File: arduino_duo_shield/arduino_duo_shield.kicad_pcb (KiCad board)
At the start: 2 copper layers, 102.1 x 119.4 mm, 70 parts, among them J2 EStop, J3 Motor_Control, J4 Limit_Switches, J5 inverter_freq, J6 inverter_cmd, J8 inverter_power, J9 Motor_Control_Mirror, K2 JQC-3F, K3 JQC-3F, P10 Digital, P11 PWM, P12 PWM, P13 Communication, P7 Power, P8 Analog, P9 Analog, Q3 2N7000, Q4 BS250, Q5 2N7000, Q6 2N7000, SW1 SW_Push, U1 4504, U2 4504, U4 74HC14, U6 74HC14, U7 PC817, U8 PC817, U9 PC817

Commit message: Generate gerber files for 1.0-alpha-1
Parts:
- added D1: LED, LED_THT:LED_D3.0mm, F.Cu at (122.9, 42.2)
- R21: value 10K -> 1K5
- moved R21 8.38 mm to (130.0, 47.2), turned to 90 degrees
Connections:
- R21 pad 1: /Spindle_VFD_Control/I_PWRSAFE -> Net-(D1-Pad1)
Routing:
- net /Spindle_VFD_Control/I_PWRSAFE: track 0.00 -> 17.3 mm
- net Net-(D1-Pad1): track 0.00 -> 9.89 mm
- net Net-(Q3-Pad2): track 25.7 -> 29.2 mm
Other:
- board text added: "ACT"
- board text removed: "EN"
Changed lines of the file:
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@@
     (thickness 1.6)
     (drawings 79)
-    (tracks 549)
+    (tracks 563)
     (zones 0)
-    (modules 70)
-    (nets 132)
+    (modules 71)
+    (nets 133)
   )
   (page A4)
@@
       (drillshape 0)
       (scaleselection 1)
-      (outputdirectory "plot/gerber"))
+      (outputdirectory "plot/1.0-alpha-1/"))
   )
   (net 0 "")
@@
   (net 130 "Net-(R24-Pad2)")
   (net 131 /Spindle_VFD_Control/I_PWRSAFE)
+  (net 132 "Net-(D1-Pad1)")
   (net_class Default "This is the default net class."
     (clearance 0.2)
@@
     (add_net "Net-(C8-Pad1)")
     (add_net "Net-(C9-Pad2)")
+    (add_net "Net-(D1-Pad1)")
     (add_net "Net-(D3-Pad2)")
     (add_net "Net-(D4-Pad2)")
@@
     (add_net /Debounce_x6/SWZmin+)
   )
+  (module LED_THT:LED_D3.0mm (layer F.Cu)
+    (at 122.936 42.164 90)
+    (descr "LED, diameter 3.0mm, 2 pins")
+    (tags "LED diameter 3.0mm 2 pins")
+    (fp_text reference D1 (at 1.27 -2.96 90) (layer F.SilkS) hide
+      (effects (font (size 1 1) (thickness 0.15)))
+    )
+    (fp_text value LED (at 1.27 2.96 90) (layer F.Fab)
+      (effects (font (size 1 1) (thickness 0.15)))
+    )
+    (fp_line (start 3.7 -2.25) (end -1.15 -2.25) (layer F.CrtYd) (width 0.05))
+    (fp_line (start 3.7 2.25) (end 3.7 -2.25) (layer F.CrtYd) (width 0.05))
+    (fp_line (start -1.15 2.25) (end 3.7 2.25) (layer F.CrtYd) (width 0.05))
+    (fp_line (start -1.15 -2.25) (end -1.15 2.25) (layer F.CrtYd) (width 0.05))
+    (fp_line (start -0.29 1.08) (end -0.29 1.236) (layer F.SilkS) (width 0.12))
+    (fp_line (start -0.29 -1.236) (end -0.29 -1.08) (layer F.SilkS) (width 0.12))
+    (fp_line (start -0.23 -1.16619) (end -0.23 1.16619) (layer F.Fab) (width 0.1))
+    (fp_circle (center 1.27 0) (end 2.77 0) (layer F.Fab) (width 0.1))
+    (fp_arc (start 1.27 0) (end 0.229039 1.08) (angle -87.9) (layer F.SilkS) (width 0.12))
+    (fp_arc (start 1.27 0) (end 0.229039 -1.08) (angle 87.9) (layer F.SilkS) (width 0.12))
+    (fp_arc (start 1.27 0) (end -0.29 1.235516) (angle -108.8) (layer F.SilkS) (width 0.12))
+    (fp_arc (start 1.27 0) (end -0.29 -1.235516) (angle 108.8) (layer F.SilkS) (width 0.12))
+    (fp_arc (start 1.27 0) (end -0.23 -1.16619) (angle 284.3) (layer F.Fab) (width 0.1))
+    (pad 2 thru_hole circle (at 2.54 0 90) (size 1.8 1.8) (drill 0.9) (layers *.Cu *.Mask)
+      (net 131 /Spindle_VFD_Control/I_PWRSAFE))
+    (pad 1 thru_hole rect (at 0 0 90) (size 1.8 1.8) (drill 0.9) (layers *.Cu *.Mask)
+      (net 132 "Net-(D1-Pad1)"))
+    (model ${KISYS3DMOD}/LED_THT.3dshapes/LED_D3.0mm.wrl
+      (at (xyz 0 0 0))
+      (scale (xyz 1 1 1))
+      (rotate (xyz 0 0 0))
+    )
+  )
   (module Relay_THT:Relay_SPDT_SANYOU_SRD_Series_Form_C (layer F.Cu)
     (at 162.052 58.42)
@@
   )
   (module Resistor_THT:R_Axial_DIN0207_L6.3mm_D2.5mm_P7.62mm_Horizontal (layer F.Cu)
-    (at 128.016 39.116 270)
+    (at 130.048 47.244 90)
     (descr "Resistor, Axial_DIN0207 series, Axial, Horizontal, pin pitch=7.62mm, 0.25W = 1/4W, length*diameter=6.3*2.5mm^2, http://cdn-reichelt.de/documents/datenblatt/B400/1_4W%23YAG.pdf")
     (tags "Resistor Axial_DIN0207 series Axial Horizontal pin pitch 7.62mm 0.25W = 1/4W length 6.3mm diameter 2.5mm")
@@
       (effects (font (size 1 1) (thickness 0.15)))
     )
-    (fp_text value 10K (at 3.81 2.37 90) (layer F.SilkS)
+    (fp_text value 1K5 (at 3.81 2.37 90) (layer F.SilkS)
       (effects (font (size 1 1) (thickness 0.15)))
     )
@@
     (fp_line (start 0.66 1.25) (end 6.96 1.25) (layer F.Fab) (width 0.1))
     (fp_line (start 0.66 -1.25) (end 0.66 1.25) (layer F.Fab) (width 0.1))
-    (pad 2 thru_hole oval (at 7.62 0 270) (size 1.6 1.6) (drill 0.8) (layers *.Cu *.Mask)
+    (pad 2 thru_hole oval (at 7.62 0 90) (size 1.6 1.6) (drill 0.8) (layers *.Cu *.Mask)
       (net 125 "Net-(Q3-Pad2)"))
-    (pad 1 thru_hole circle (at 0 0 270) (size 1.6 1.6) (drill 0.8) (layers *.Cu *.Mask)
-      (net 131 /Spindle_VFD_Control/I_PWRSAFE))
+    (pad 1 thru_hole circle (at 0 0 90) (size 1.6 1.6) (drill 0.8) (layers *.Cu *.Mask)
+      (net 132 "Net-(D1-Pad1)"))
     (model ${KISYS3DMOD}/Resistor_THT.3dshapes/R_Axial_DIN0207_L6.3mm_D2.5mm_P7.62mm_Horizontal.wrl
       (at (xyz 0 0 0))
@@
     )
   )
+  (gr_text ACT (at 119.888 40.64 90) (layer F.SilkS)
+    (effects (font (size 1 1) (thickness 0.15)))
+  )
   (gr_text "Itadinanta CNC Board\nfor Arduino Due\n1.0-alpha-1-2019-12-28" (at 153.416 134.62 90) (layer F.SilkS)
     (effects (font (size 1 1) (thickness 0.15)))
@@
     (effects (font (size 1 1) (thickness 0.15)))
   )
-  (gr_text EN (at 181.864 62.992 90) (layer F.SilkS)
-    (effects (font (size 1 1) (thickness 0.15)))
-  )
   (gr_text NO (at 181.864 49.784 90) (layer F.SilkS)
     (effects (font (size 1 1) (thickness 0.15)))
@@
   (segment (start 146.812 41.656) (end 149.86 38.608) (width 0.25) (layer F.Cu) (net 124))
   (segment (start 138.684 41.656) (end 146.812 41.656) (width 0.25) (layer F.Cu) (net 124))
-  (segment (start 128.016 52.324) (end 128.016 46.736) (width 0.25) (layer F.Cu) (net 125))
   (segment (start 137.684 40.386) (end 136.652 41.418) (width 0.25) (layer F.Cu) (net 125))
   (segment (start 138.684 40.386) (end 137.684 40.386) (width 0.25) (layer F.Cu) (net 125))
   (segment (start 137.684 49.022) (end 138.684 49.022) (width 0.25) (layer F.Cu) (net 125))
-  (segment (start 136.652 47.99) (end 137.684 49.022) (width 0.25) (layer F.Cu) (net 125))
-  (segment (start 128.016 46.736) (end 136.652 46.736) (width 0.25) (layer F.Cu) (net 125))
-  (segment (start 136.652 41.418) (end 136.652 46.736) (width 0.25) (layer F.Cu) (net 125))
   (segment (start 136.652 46.736) (end 136.652 47.99) (width 0.25) (layer F.Cu) (net 125))
+  (segment (start 132.71641 41.656) (end 130.366205 39.305795) (width 0.25) (layer F.Cu) (net 125))
+  (segment (start 136.652 41.656) (end 132.71641 41.656) (width 0.25) (layer F.Cu) (net 125))
+  (segment (start 136.652 41.656) (end 136.652 46.736) (width 0.25) (layer F.Cu) (net 125))
+  (segment (start 136.652 41.418) (end 136.652 41.656) (width 0.25) (layer F.Cu) (net 125))
+  (segment (start 132.08 48.26) (end 136.652 48.26) (width 0.25) (layer F.Cu) (net 125))
+  (segment (start 128.016 52.324) (end 132.08 48.26) (width 0.25) (layer F.Cu) (net 125))
+  (segment (start 136.652 47.99) (end 136.652 48.26) (width 0.25) (layer F.Cu) (net 125))
+  (segment (start 136.652 48.26) (end 137.684 49.022) (width 0.25) (layer F.Cu) (net 125))
   (segment (start 109.22 52.324) (end 113.284 52.324) (width 0.25) (layer F.Cu) (net 126))
   (segment (start 119.997001 45.610999) (end 114.083999 51.524001) (width 0.25) (layer B.Cu) (net 126))
@@
   (segment (start 116.84 60.452) (end 117.348 59.944) (width 0.25) (layer F.Cu) (net 130))
   (segment (start 116.84 63.5) (end 116.84 60.452) (width 0.25) (layer F.Cu) (net 130))
+  (segment (start 138.176 39.116) (end 138.684 39.116) (width 0.25) (layer F.Cu) (net 131))
+  (segment (start 123.835999 38.724001) (end 122.936 39.624) (width 0.25) (layer F.Cu) (net 131))
+  (segment (start 136.668 38.1) (end 124.46 38.1) (width 0.25) (layer F.Cu) (net 131))
+  (segment (start 124.46 38.1) (end 123.835999 38.724001) (width 0.25) (layer F.Cu) (net 131))
+  (segment (start 138.684 39.116) (end 137.684 39.116) (width 0.25) (layer F.Cu) (net 131))
+  (segment (start 137.684 39.116) (end 136.668 38.1) (width 0.25) (layer F.Cu) (net 131))
+  (segment (start 126.866 47.244) (end 128.91663 47.244) (width 0.25) (layer F.Cu) (net 132))
+  (segment (start 122.936 43.314) (end 126.866 47.244) (width 0.25) (layer F.Cu) (net 132))
+  (segment (start 128.91663 47.244) (end 130.048 47.244) (width 0.25) (layer F.Cu) (net 132))
+  (segment (start 122.936 42.164) (end 122.936 43.314) (width 0.25) (layer F.Cu) (net 132))
   (zone (net 1) (net_name GND) (layer B.Cu) (hatch edge 0.508)
     (connect_pads (clearance 0.508))

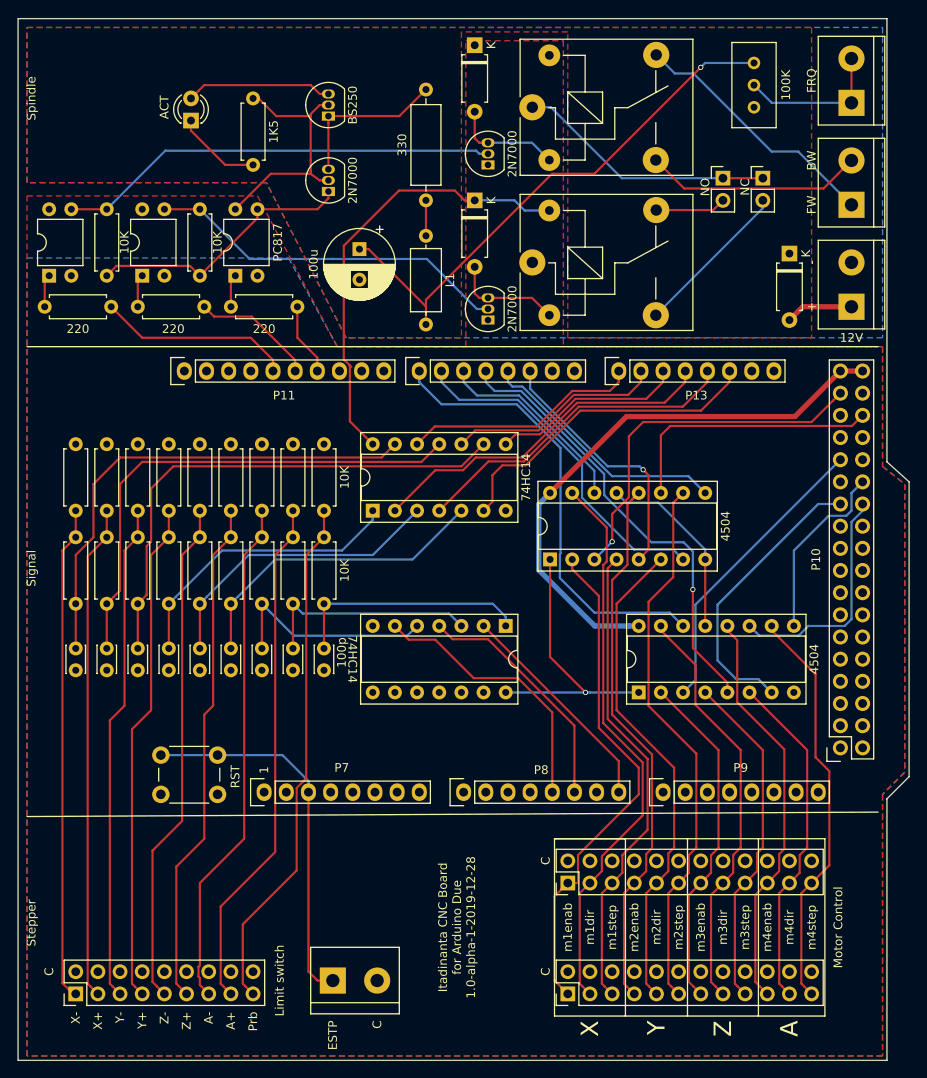
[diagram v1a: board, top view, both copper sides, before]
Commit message: Add voltage follower as end stage of spindle control
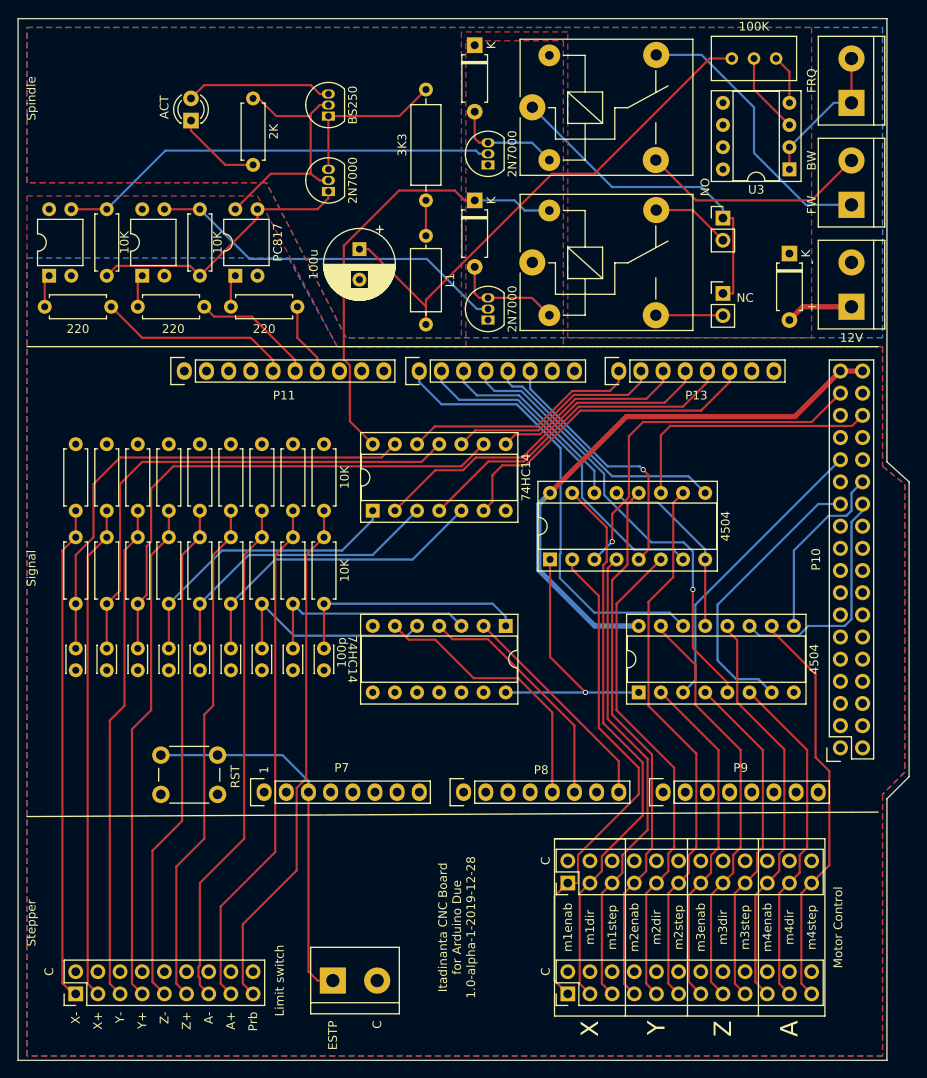
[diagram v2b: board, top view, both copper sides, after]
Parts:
- added U3: LM358, Package_DIP:DIP-8_W7.62mm_Socket, F.Cu at (191.5, 47.8)
- R21: value 1K5 -> 2K
- R23: value 330 -> 3K3
- moved JP2 14.0 mm to (183.9, 62.0)
- moved JP3 4.57 mm to (183.9, 53.3)
- moved RV1 2.59 mm to (184.9, 35.1), turned to 180 degrees
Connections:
- RV1 pad 2: /Spindle_VFD_Control/inverter_frequency_10V -> Net-(RV1-Pad2)
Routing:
- net Net-(JP2-Pad2): track 18.2 -> 7.71 mm
- net Net-(RV1-Pad2): track 0.00 -> 9.30 mm
- net Net-(JP2-Pad1): track 29.8 -> 38.6 mm
- net /Spindle_VFD_Control/inverter_gnd: track 31.4 -> 37.1 mm
- net /Spindle_VFD_Control/inverter_fw_switch: track 29.5 -> 32.6 mm
- net Net-(C8-Pad1): track 62.0 -> 59.7 mm, vias 1 -> 0
- net /Spindle_VFD_Control/inverter_bw_switch: track 25.1 -> 26.2 mm
- net Net-(JP3-Pad2): track 8.10 -> 9.08 mm

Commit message: Expose raw analog frequency control
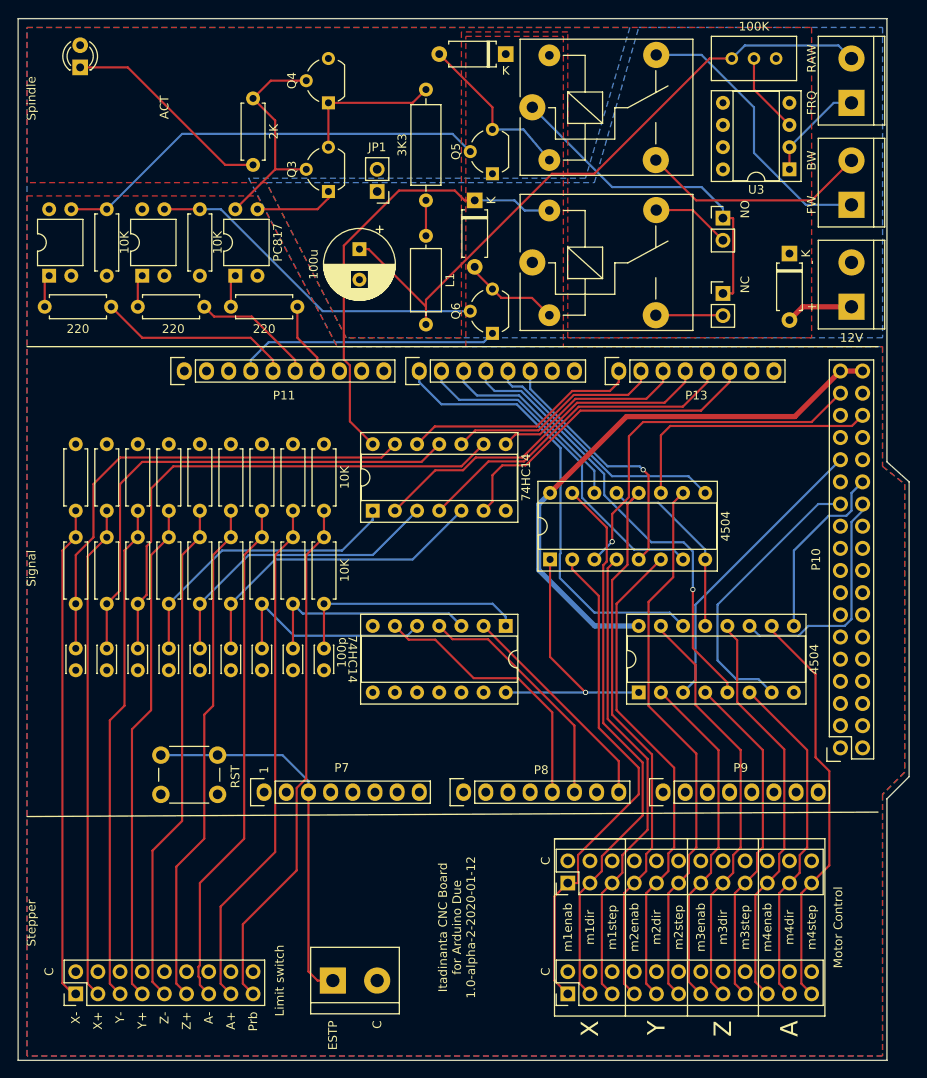
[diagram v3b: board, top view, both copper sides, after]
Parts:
- added JP1: Jumper_NC_Small, Connector_PinHeader_2.54mm:PinHeader_1x02_P2.54mm_Vertical, F.Cu at (144.3, 50.3)
- Q3, Q4, Q5, Q6: footprint Package_TO_SOT_THT:TO-92_Inline -> Package_TO_SOT_THT:TO-92_Wide
- moved D1 14.1 mm to (110.2, 36.1)
- moved D3 3.70 mm to (159.0, 34.5), turned to 180 degrees
- moved Q6 1.61 mm to (157.5, 66.5)
- moved Q4 1.52 mm to (138.7, 40.1)
- moved Q5 1.14 mm to (157.5, 48.3)
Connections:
- C8 pad 1: Net-(C8-Pad1) -> /Spindle_VFD_Control/inverter_frequency_raw_10V
- J5 pad 2: /Spindle_VFD_Control/inverter_frequency_10V -> /Spindle_VFD_Control/inverter_frequency_raw_10V
- L1 pad 2: Net-(C8-Pad1) -> /Spindle_VFD_Control/inverter_frequency_raw_10V
- Q5 pad 1: /Spindle_VFD_Control/inverter_gnd -> GND
- Q6 pad 1: /Spindle_VFD_Control/inverter_gnd -> GND
- R25 pad 2: /Spindle_VFD_Control/inverter_gnd -> GND
- R26 pad 2: /Spindle_VFD_Control/inverter_gnd -> GND
- RV1 pad 1: Net-(C8-Pad1) -> /Spindle_VFD_Control/inverter_frequency_raw_10V
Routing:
- net /Spindle_VFD_Control/inverter_frequency_raw_10V: track 0.00 -> 74.6 mm
- net Net-(C8-Pad1): track 59.7 -> 0.00 mm
- net GND: track 21.6 -> 51.8 mm
- net /Spindle_VFD_Control/inverter_gnd: track 37.1 -> 9.42 mm
- net /Spindle_VFD_Control/I_PWRSAFE: track 17.3 -> 0.00 mm
- net Net-(D1-Pad1): track 9.89 -> 24.4 mm
- net Net-(D3-Pad2): track 12.6 -> 19.8 mm
- net /Spindle_VFD_Control/inverter_frequency_10V: track 16.8 -> 11.8 mm
- net Net-(Q3-Pad2): track 29.2 -> 25.7 mm
- net Net-(Q6-Pad2): track 42.0 -> 39.9 mm
- net Net-(Q3-Pad3): track 18.5 -> 16.9 mm
- net Net-(D4-Pad2): track 12.6 -> 11.1 mm
- net Net-(Q5-Pad2): track 50.7 -> 50.1 mm
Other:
- board text added: "Itadinanta CNC Board for Arduino Due 1.0-alpha-2-2020-01-12"
- board text added: "RAW"
- board text removed: "Itadinanta CNC Board for Arduino Due 1.0-alpha-1-2019-12-28"

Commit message: Add support for spindle estop
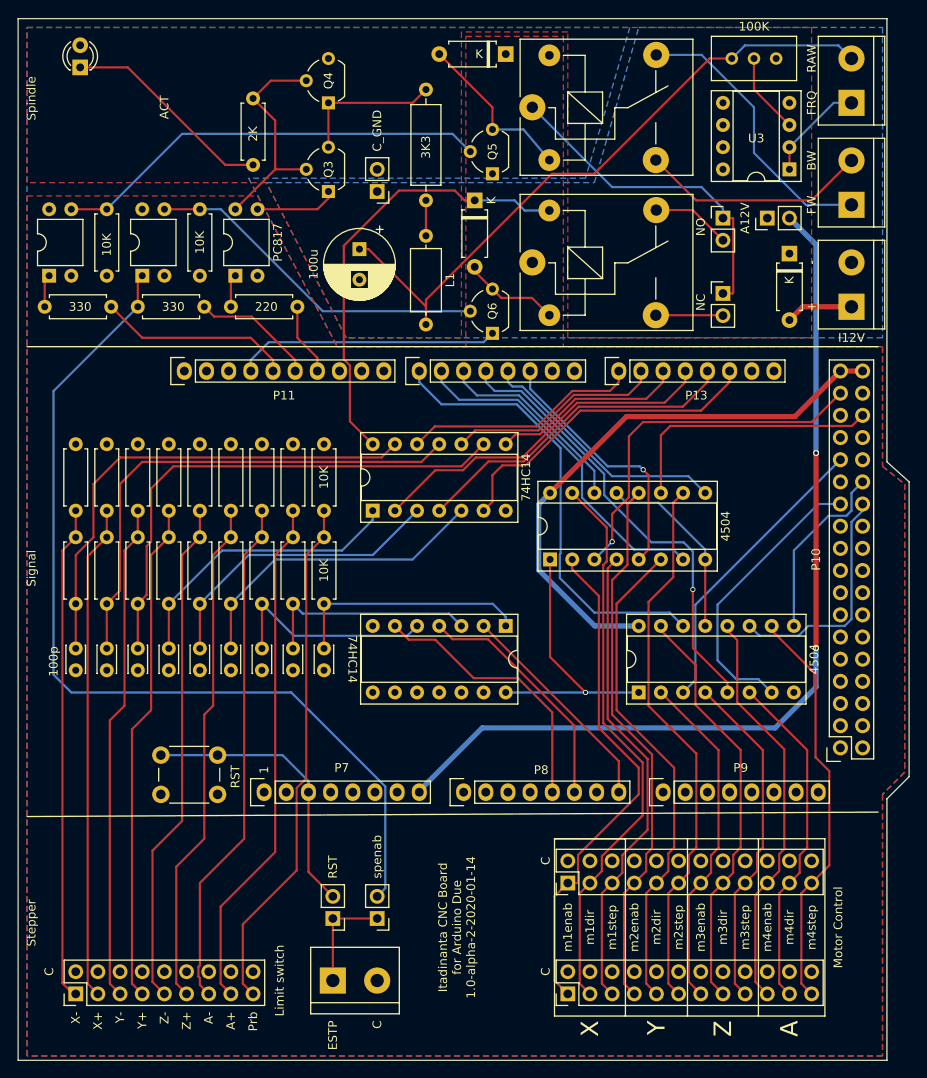
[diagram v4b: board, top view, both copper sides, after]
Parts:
- added JP4: Jumper_NC_Small, Connector_PinHeader_2.54mm:PinHeader_1x02_P2.54mm_Vertical, F.Cu at (189.0, 53.3)
- added JP5: EStop_RST, Connector_PinHeader_2.54mm:PinHeader_1x02_P2.54mm_Vertical, F.Cu at (139.2, 133.6)
- added JP6: EStop_spenab, Connector_PinHeader_2.54mm:PinHeader_1x02_P2.54mm_Vertical, F.Cu at (144.3, 133.6)
- R22, R24: value 220 -> 330
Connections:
- net Net-(R24-Pad2) renamed /Spindle_VFD_Control/ext_estop
- J2 pad 1: /Reset -> Net-(J2-Pad1)
- P7 pad 8: /Vin -> ext_12v
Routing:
- net ext_12v: track 0.00 -> 105.5 mm, vias 0 -> 2
- net /Spindle_VFD_Control/ext_estop: track 3.77 -> 106.2 mm
- net Net-(J2-Pad1): track 0.00 -> 12.2 mm
- net /Reset: track 43.2 -> 32.5 mm
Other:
- board text added: "A12V"
- board text added: "C_GND"
- board text added: "I12V"
- board text added: "Itadinanta CNC Board for Arduino Due 1.0-alpha-2-2020-01-14"
- board text added: "spenab"
- board text removed: "12V"
- board text removed: "Itadinanta CNC Board for Arduino Due 1.0-alpha-2-2020-01-12"
